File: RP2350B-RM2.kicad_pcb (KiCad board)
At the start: 2 copper layers, 52 x 71.5 mm, 49 parts, among them J1 10103594-0001LF, J2 TSW-126-07-L-D, J3 TSW-126-07-L-D, J4 SM03B-SRSS-TB(LF)(SN), SW1 434133025816, SW2 434133025816, U1 RP2350B, U2 NCP1117ST33T3G, U3 W25Q128JVSIQ, U4 W25Q128JVSIQ, X1 12MHz

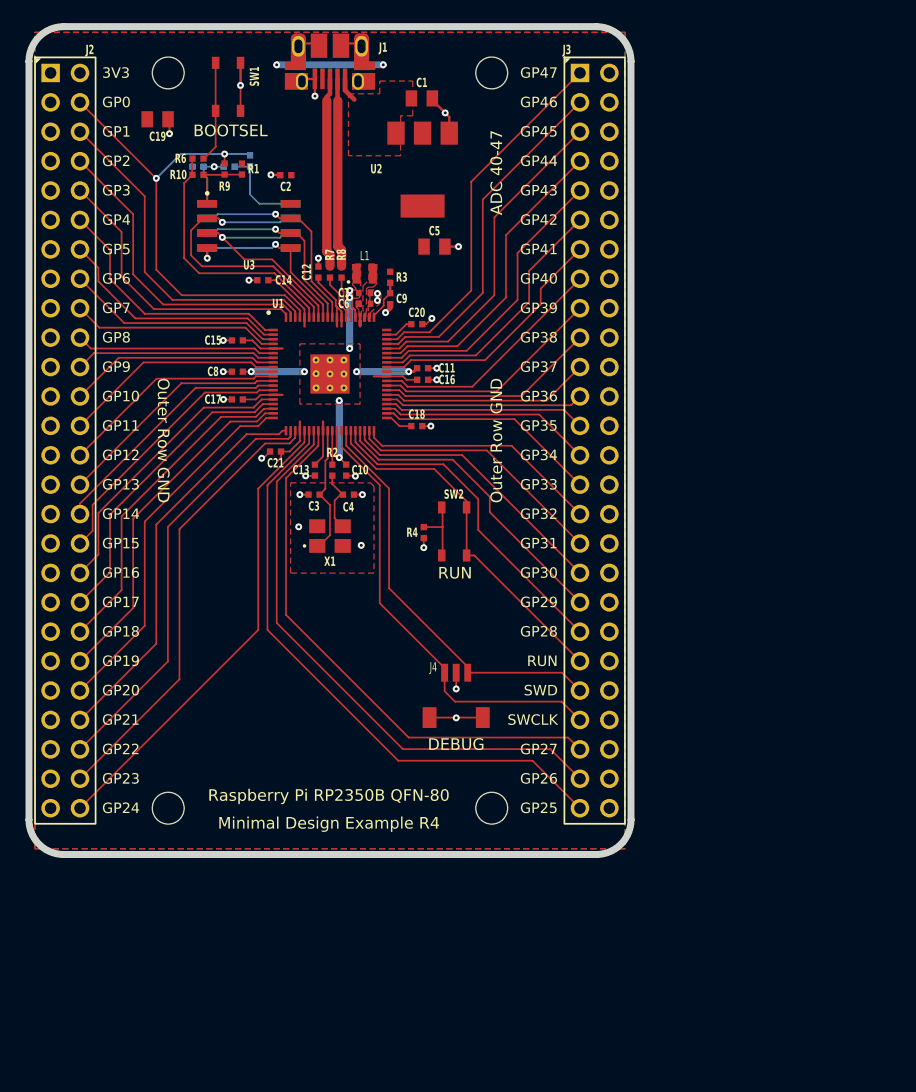
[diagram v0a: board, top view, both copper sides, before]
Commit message: Lay out RM2 radio and APS6404L PSRAM on Pi's board
Update PCB from Schematic (scripted, KiCad 10.0.6), then:

- Add a 22.5 x 27.5 mm tab on the right edge for the RM2. The antenna end
  faces the tab edge, with a copper-free rule area on both layers across
  the whole antenna strip. The module has GND pours under it and a via at
  every GND pad. gSPI runs from J3's GPIO43-46 between the outer GND pins.
  3V3 comes from Pi's pour strip beside J3.
- Swap U4 to a 150 mil SOIC-8 and replace its back-side fan-out, whose vias
  sat under the new pads.
- Move R11 from GPIO0 to GPIO47.

Pi's other footprints and tracks are unchanged. DRC shows 0 unconnected
items and 0 parity issues; only Pi's RPI_COMPILED library notes remain.

Co-Authored-By: Claude Opus 5.5 <noreply@anthropic.com>
Claude-Session: https://claude.ai/code/session_01TVxWe2rd4mhh6Q8D57QZer
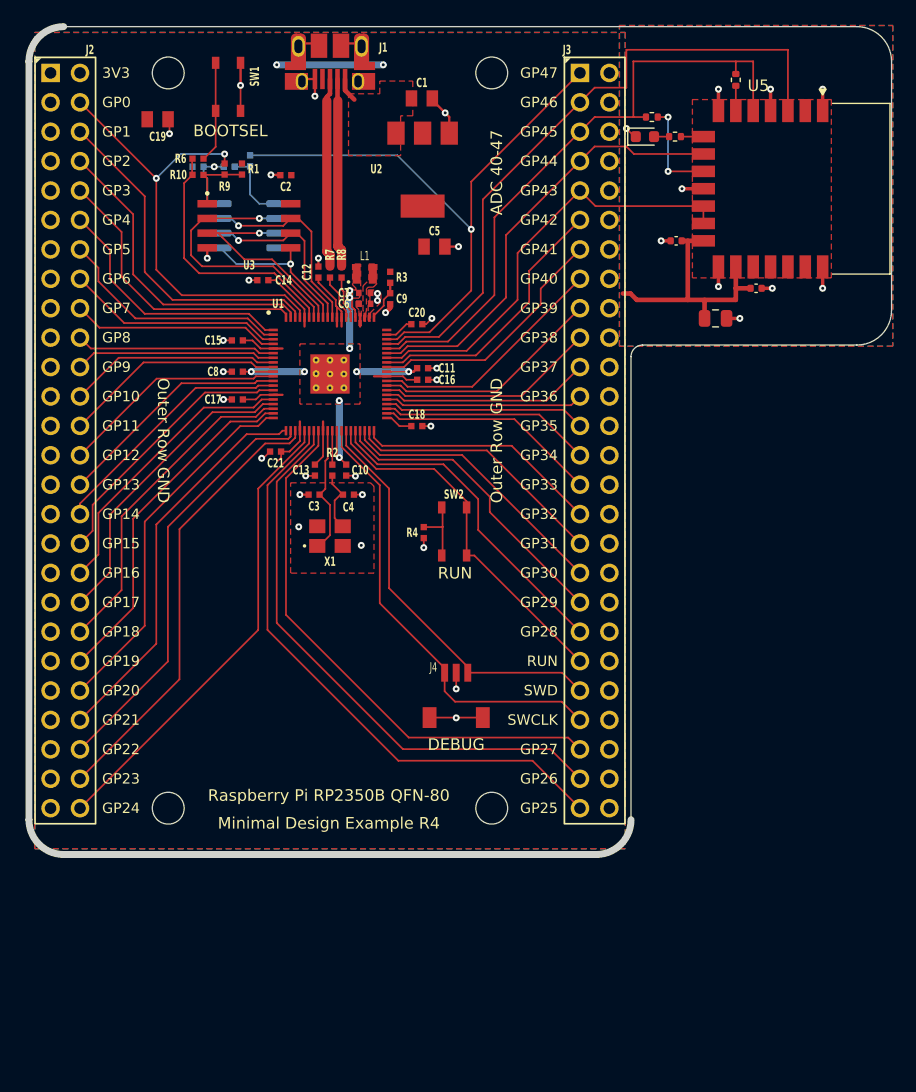
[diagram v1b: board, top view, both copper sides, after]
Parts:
- added C23: 10u, Capacitor_SMD:C_0805_2012Metric, F.Cu at (133.3, 95.2)
- added C24: 100n, Capacitor_SMD:C_0402_1005Metric, F.Cu at (136.8, 92.6)
- added C25: 100n, Capacitor_SMD:C_0402_1005Metric, F.Cu at (129.9, 88.5)
- added D1: Green, LED_SMD:LED_0603_1608Metric, F.Cu at (127.2, 79.5)
- added R14: 470, Resistor_SMD:R_0402_1005Metric, F.Cu at (135.1, 74.6)
- added R15: 10k, Resistor_SMD:R_0402_1005Metric, F.Cu at (127.8, 77.8)
- added R16: 1k, Resistor_SMD:R_0402_1005Metric, F.Cu at (129.8, 79.5)
- added U5: RM2, rp2350b_rm2:RPi_RM2, F.Cu at (140.0, 84.0)
- U4: value W25Q128JVSIQ -> APS6404L-3SQR-SN; footprint RPI_COMPILED:generic_soic127p790x195-8 -> Package_SO:SOIC-8_3.9x4.9mm_P1.27mm
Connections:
- net /FLASH2_SS renamed /PSRAM_CS
- R11 pad 1: /GPIO0 -> /GPIO47_ADC7
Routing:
- net /GPIO46_ADC6: track 30.1 -> 57.1 mm
- net /GPIO45_ADC5: track 28.4 -> 55.1 mm
- net +3V3: track 52.9 -> 76.7 mm
- net /GPIO47_ADC7: track 31.7 -> 53.5 mm, vias 0 -> 1
- net GND: track 38.8 -> 53.8 mm, vias 29 -> 39
- net /GPIO43_ADC3: track 25.0 -> 37.8 mm
- net /GPIO44_ADC4: track 26.7 -> 38.2 mm
- net Net-(U5-~{IRQ}): track 0.00 -> 8.63 mm, vias 0 -> 2
- net /GPIO0: track 41.5 -> 39.2 mm
- net Net-(U5-DO): track 0.00 -> 2.14 mm
- net Net-(U5-GPIO0): track 0.00 -> 1.94 mm
- net /QSPI_SD1: track 24.8 -> 23.4 mm
- net Net-(D1-A): track 0.00 -> 1.30 mm
- net /PSRAM_CS: track 7.52 -> 6.40 mm
- net /QSPI_SD2: track 19.3 -> 18.3 mm
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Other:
- board size 52 x 71.5 mm -> 74.5 x 71.5 mm

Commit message: Move the RM2 to a stretched end of the board instead of a side tab
Drop the right-hand tab. The board keeps its 52 mm width and grows 18 mm
at the end away from USB, as on the Pico 2 W. The RM2 sits between the
headers there with its antenna at the new bottom edge, and a full-width
rule area keeps copper off both layers under the antenna.

GPIO43-46 run down J3 on the top layer, in the gap between its pin
columns and between its GND column and the edge, where Pi has no copper.
IRQ is the only radio signal that takes the back layer. Each GND pad
still gets its own via. The U4 and R11 changes are as before.

DRC: 0 unconnected items, 0 parity issues; only Pi's RPI_COMPILED
library notes remain.

Co-Authored-By: Claude Opus 5.5 <noreply@anthropic.com>
Claude-Session: https://claude.ai/code/session_01TVxWe2rd4mhh6Q8D57QZer
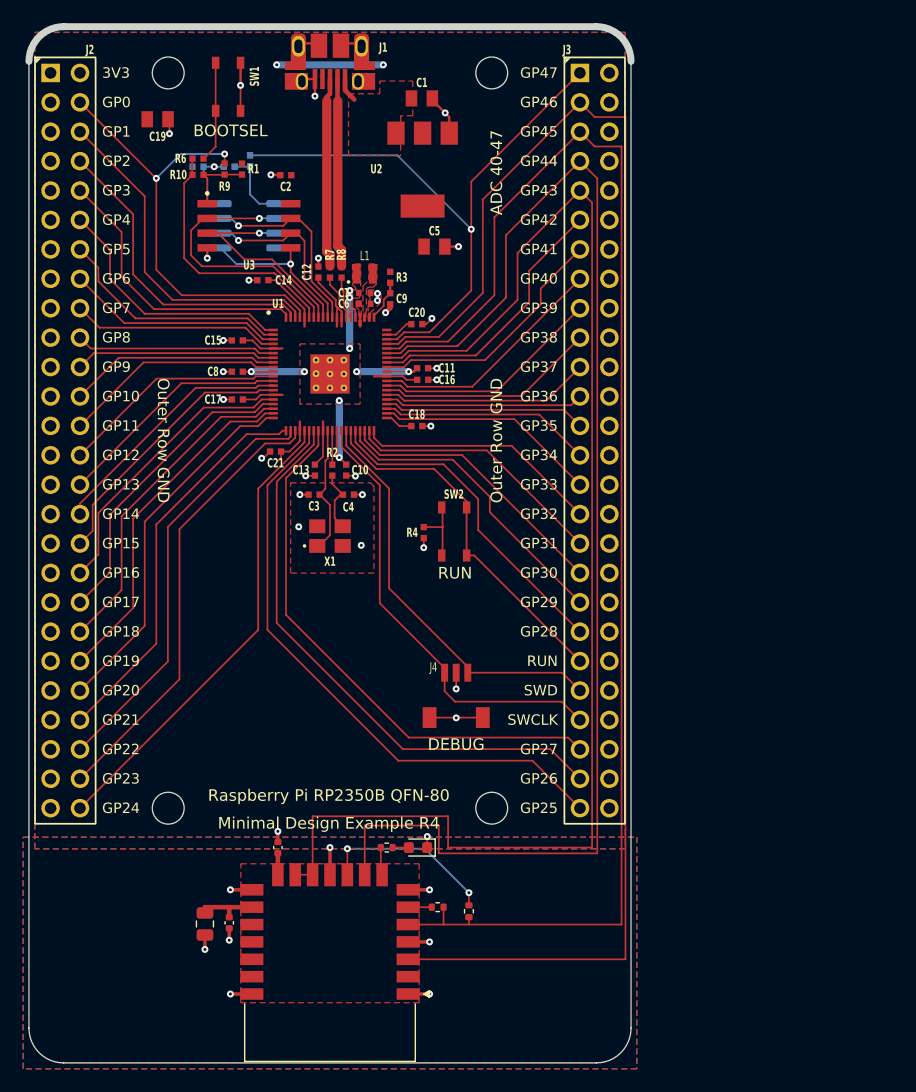
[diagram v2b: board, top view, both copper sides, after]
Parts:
- moved U5 78.0 mm to (100.0, 151.0), turned to 180 degrees
- moved R14 75.9 mm to (109.3, 146.1), turned to 180 degrees
- moved C24 71.2 mm to (91.3, 147.4), turned to -90 degrees
- moved R15 70.4 mm to (112.0, 146.4), turned to 90 degrees
- moved C23 68.4 mm to (89.2, 147.5), turned to -90 degrees
- moved R16 66.3 mm to (104.9, 140.9), turned to 0 degrees
- moved D1 64.5 mm to (107.6, 140.9), turned to 180 degrees
- moved C25 62.7 mm to (95.5, 140.9), turned to 90 degrees
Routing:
- net /GPIO43_ADC3: track 37.8 -> 115.6 mm
- net /GPIO44_ADC4: track 38.2 -> 113.9 mm
- net /GPIO46_ADC6: track 57.1 -> 126.0 mm
- net /GPIO45_ADC5: track 55.1 -> 120.3 mm
- net +3V3: track 76.7 -> 61.4 mm
- net Net-(U5-~{IRQ}): track 8.63 -> 15.4 mm
- net GND: track 53.8 -> 54.6 mm
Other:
- board size 74.5 x 71.5 mm -> 52 x 89.5 mm

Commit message: Add 3V3 header extensions J5/J6 and move the bottom mounting holes
Schematic: add J5 and J6, 2x02 headers that continue J2 and J3 by two
rows. Each has two 3V3 pins on the inner column and two GND pins on the
outer column, matching how J2/J3 are laid out. New footprint
PinHeader_2x02_P2.54mm_Ext: round pads, with silkscreen that joins the
header outline above.

Board: J5/J6 sit on J2/J3's 2.54 mm grid with "3V3" labels in Pi's
style. The WL_ON and CS lanes now turn below them, and J6's 3V3 pins get
a track into the pour. MH3/MH4 move to the new end, in line with the top
pair and 4 mm from the edge, so the holes form a 27.94 x 81.5 mm
rectangle. The antenna rule area allows the NPTH holes.

DRC: 0 unconnected items, 0 parity issues; only Pi's RPI_COMPILED
library notes. ERC: unchanged (4 pre-existing items).

Co-Authored-By: Claude Opus 5.5 <noreply@anthropic.com>
Claude-Session: https://claude.ai/code/session_01TVxWe2rd4mhh6Q8D57QZer
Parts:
- added J5: Conn_02x02, rp2350b_rm2:PinHeader_2x02_P2.54mm_Ext, F.Cu at (75.9, 140.0)
- added J6: Conn_02x02, rp2350b_rm2:PinHeader_2x02_P2.54mm_Ext, F.Cu at (121.6, 140.0)
- moved MH3 18.0 mm to (114.0, 155.5)
- moved MH4 18.0 mm to (86.0, 155.5)
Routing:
- net /GPIO44_ADC4: track 113.9 -> 119.9 mm
- net /GPIO43_ADC3: track 115.6 -> 121.6 mm
- net +3V3: track 61.4 -> 65.9 mm
- net Net-(U5-~{IRQ}): track 15.4 -> 16.8 mm

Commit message: Single-row J2/J3 headers with 3V3 and GND at the ends
Replace Pi's 2x26 headers (outer column all GND) and the J5/J6
extensions with single-row headers on Pi's signal columns:
  J2 (1x29): 3V3, GPIO0-24, GND, 3V3, GND
  J3 (1x28): 3V3, 3V3, GND x3, GPIO42-28, RUN, SWD, SWCLK,
             GPIO27-25, 3V3, GND
GPIO43-47 leave the header, since the radio and PSRAM need them.

Schematic: new Conn_01x29 / Conn_01x28 symbols sit exactly on the old
signal-pin positions, so every GPIO label connection carries over.
The GND buses, J5/J6 and the GPIO43-47 header hookups are removed.

Board: stock PinHeader_1x29/1x28 footprints on the same pads, so Pi's
routing to every GPIO is untouched. Pi's GPIO43-46 runs stop short of
J3's new power pins and slip between them into four lanes where the
outer column was. GPIO47 stops at the via to R11. J3's top 3V3 pins
join the pour by U2. Silkscreen: J3's top labels now read 3V3/GND,
"ADC 40-42", and the "Outer Row GND" notes are gone. The J5/J6
footprint is removed.

DRC: 0 unconnected items, 0 parity issues, only Pi's 46 RPI_COMPILED
library notes. ERC unchanged (4 pre-existing items). U2 to the RM2's
VIN is now about 15 mOhm, down from 19.

Co-Authored-By: Claude Opus 5.5 <noreply@anthropic.com>
Claude-Session: https://claude.ai/code/session_01TVxWe2rd4mhh6Q8D57QZer
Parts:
- removed J5, J6: Conn_02x02, rp2350b_rm2:PinHeader_2x02_P2.54mm_Ext
- J2: value TSW-126-07-L-D -> Conn_01x29; footprint RPI_COMPILED:samtec_tsw-126-07-l-d -> Connector_PinHeader_2.54mm:PinHeader_1x29_P2.54mm_Vertical
- J3: value TSW-126-07-L-D -> Conn_01x28; footprint RPI_COMPILED:samtec_tsw-126-07-l-d -> Connector_PinHeader_2.54mm:PinHeader_1x28_P2.54mm_Vertical
- moved J2 31.8 mm to (78.4, 74.0), turned to 0 degrees
- moved J3 31.8 mm to (121.6, 74.0), turned to 0 degrees
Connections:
- J2 pad 1: GND -> +3V3
- J2 pad 10: /GPIO3 -> /GPIO8
- J2 pad 11: GND -> /GPIO9
- J2 pad 12: /GPIO4 -> /GPIO10
- J2 pad 13: GND -> /GPIO11
- J2 pad 14: /GPIO5 -> /GPIO12
- J2 pad 15: GND -> /GPIO13
- J2 pad 16: /GPIO6 -> /GPIO14
- J2 pad 17: GND -> /GPIO15
- J2 pad 18: /GPIO7 -> /GPIO16
- J2 pad 19: GND -> /GPIO17
- J2 pad 2: +3V3 -> /GPIO0
- J2 pad 20: /GPIO8 -> /GPIO18
- J2 pad 21: GND -> /GPIO19
- J2 pad 22: /GPIO9 -> /GPIO20
- J2 pad 23: GND -> /GPIO21
- J2 pad 24: /GPIO10 -> /GPIO22
- J2 pad 25: GND -> /GPIO23
- J2 pad 26: /GPIO11 -> /GPIO24
- J2 pad 28: /GPIO12 -> +3V3
- J2 pad 3: GND -> /GPIO1
- J2 pad 4: /GPIO0 -> /GPIO2
- J2 pad 5: GND -> /GPIO3
- J2 pad 6: /GPIO1 -> /GPIO4
- J2 pad 7: GND -> /GPIO5
- J2 pad 8: /GPIO2 -> /GPIO6
- J2 pad 9: GND -> /GPIO7
- J3 pad 1: /GPIO47_ADC7 -> +3V3
- J3 pad 10: GND -> /GPIO38
- J3 pad 11: /GPIO42_ADC2 -> /GPIO37
- J3 pad 12: GND -> /GPIO36
- J3 pad 13: /GPIO41_ADC1 -> /GPIO35
- J3 pad 14: GND -> /GPIO34
- J3 pad 15: /GPIO40_ADC0 -> /GPIO33
- J3 pad 16: GND -> /GPIO32
- J3 pad 17: /GPIO39 -> /GPIO31
- J3 pad 18: GND -> /GPIO30
- J3 pad 19: /GPIO38 -> /GPIO29
- J3 pad 2: GND -> +3V3
- J3 pad 20: GND -> /GPIO28
- J3 pad 21: /GPIO37 -> /RUN
- J3 pad 22: GND -> /SWD
- J3 pad 23: /GPIO36 -> /SWCLK
- J3 pad 24: GND -> /GPIO27
- J3 pad 25: /GPIO35 -> /GPIO26
- J3 pad 26: GND -> /GPIO25
- J3 pad 27: /GPIO34 -> +3V3
- J3 pad 3: /GPIO46_ADC6 -> GND
- J3 pad 5: /GPIO45_ADC5 -> GND
- J3 pad 6: GND -> /GPIO42_ADC2
- J3 pad 7: /GPIO44_ADC4 -> /GPIO41_ADC1
- J3 pad 8: GND -> /GPIO40_ADC0
- J3 pad 9: /GPIO43_ADC3 -> /GPIO39
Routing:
- net /GPIO47_ADC7: track 53.5 -> 36.1 mm
- net /GPIO45_ADC5: track 120.3 -> 117.5 mm
- net +3V3: track 65.9 -> 68.3 mm
- net /GPIO46_ADC6: track 126.0 -> 123.9 mm
- net /GPIO43_ADC3: track 121.6 -> 121.0 mm
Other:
- board text added: "ADC 40-42"
- board text added: "GND"
- board text removed: "ADC 40-47"
- board text removed: "GP43"
- board text removed: "GP44"
- board text removed: "GP45"
- board text removed: "GP46"
- board text removed: "GP47"
- board text removed: "Outer Row GND"
